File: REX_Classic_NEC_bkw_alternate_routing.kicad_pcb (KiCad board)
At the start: 2 copper layers, 17.8 x 35.6 mm, 9 parts, among them J1 DIP28 legs 27C256, J2 JTAG, J3 PRG, U1 XCR3064-VQ44, U2 29F800, U3 LP2980

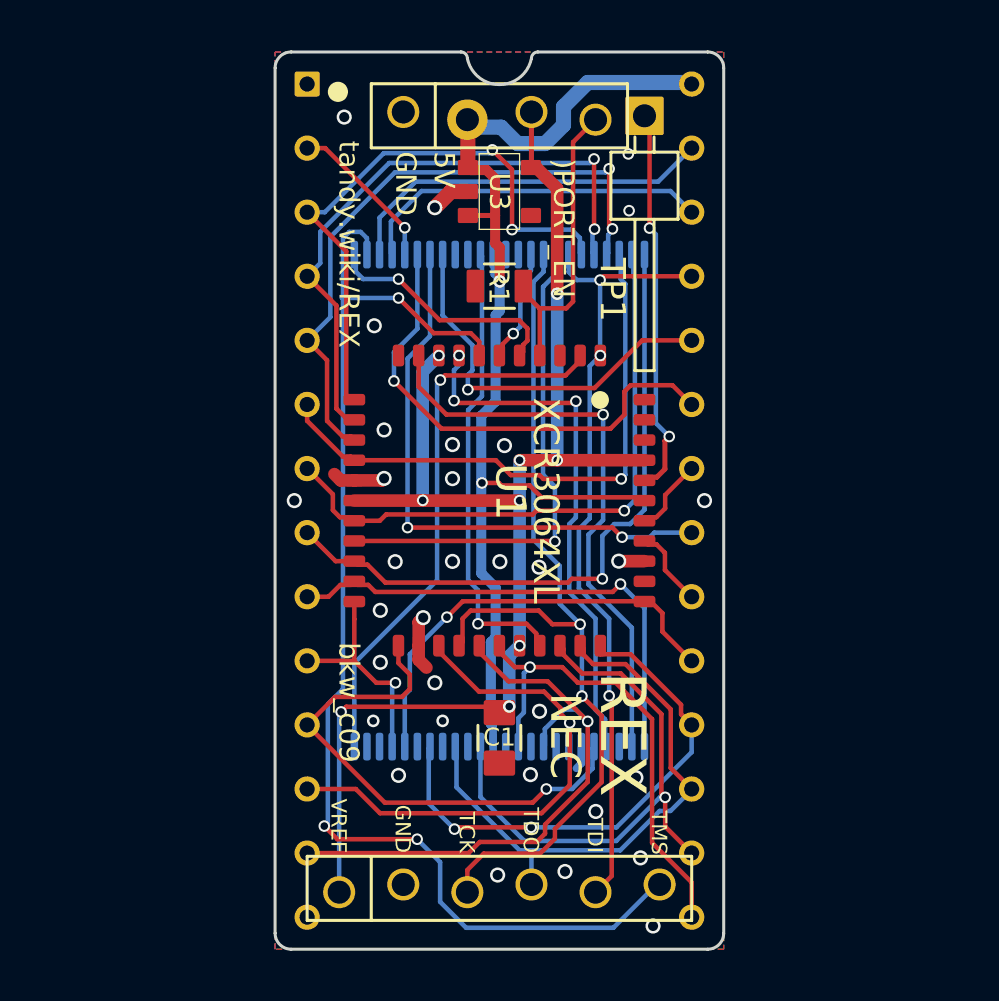
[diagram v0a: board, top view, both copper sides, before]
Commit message: small layout nudges
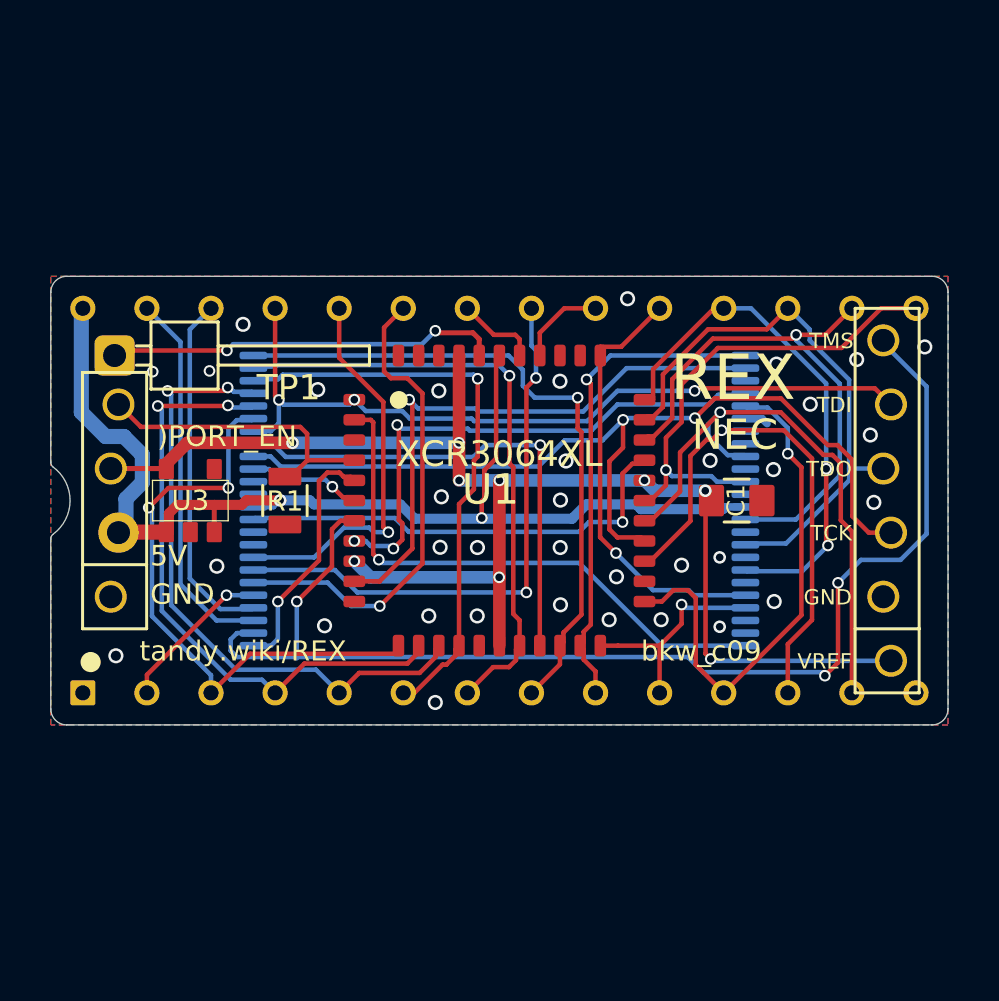
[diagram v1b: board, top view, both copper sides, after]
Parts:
- J1: footprint 000_LOCAL:DIP-28_600_pcb_2 -> 000_LOCAL:DIP-28_600_pcb_shallow_notch
- moved TP1 23.0 mm to (131.1, 89.5), turned to 0 degrees
- moved J2 21.7 mm to (161.7, 95.2), turned to 90 degrees
- moved J3 21.6 mm to (131.1, 95.2), turned to 90 degrees
- moved U3 17.3 mm to (134.1, 95.2), turned to 90 degrees
- moved C1 13.3 mm to (155.8, 95.2), turned to 0 degrees
- moved R1 12.0 mm to (137.9, 95.2), turned to 90 degrees
- turned J1 to 90 degrees
- turned U1 to 0 degrees
- turned U2 to 0 degrees
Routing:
- net GND: track 7.83 -> 0.94 mm, vias 32 -> 35
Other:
- board size 17.8 x 35.6 mm -> 35.6 x 17.8 mm
